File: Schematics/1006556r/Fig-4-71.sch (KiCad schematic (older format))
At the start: 0 parts

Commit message: For module A31, transcribed through Fig 4-87, leaving just 88, 91, 93, 114, 141, and 147 to go, plus their integration into the top-level sheet (and resolution of remaining inconsistencies in ND-1021041).
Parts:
- added J1: ConnectorGeneric, symbol AGC_DSKY:ConnectorGeneric
- added U? (x6): D3NOR-+3VDC-0VDC-nd1021041-ABC-___, symbol D3NOR-+3VDC-0VDC-nd1021041:D3NOR-+3VDC-0VDC-nd1021041-ABC-___
- added U? (x6): D3NOR-+3VDC-0VDC-nd1021041-A_C-___, symbol D3NOR-+3VDC-0VDC-nd1021041:D3NOR-+3VDC-0VDC-nd1021041-A_C-___
- added U? (x2): D3NOR-NC-0VDC-expander-nd1021041-A_C-___, symbol D3NOR-NC-0VDC-expander-nd1021041:D3NOR-NC-0VDC-expander-nd1021041-A_C-___
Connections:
- net +3VDC: now also U?.6 (+3VDC), U?.6 (+3VDC), U?.6 (+3VDC), U?.6 (+3VDC), U?.6 (+3VDC), U?.6 (+3VDC), U?.6 (+3VDC), U?.6 (+3VDC), U?.6 (+3VDC), U?.6 (+3VDC), U?.6 (+3VDC), U?.6 (+3VDC)
- net 0VDC: now also U?.3 (0VDC), U?.3 (0VDC), U?.3 (0VDC), U?.3 (0VDC), U?.3 (0VDC), U?.3 (0VDC), U?.3 (0VDC), U?.3 (0VDC), U?.5 (0VDC), U?.5 (0VDC), U?.5 (0VDC), U?.5 (0VDC), U?.5 (0VDC), U?.5 (0VDC), U?.5 (0VDC), U?.5 (0VDC), U?.5 (0VDC), U?.5 (0VDC), U?.5 (0VDC), U?.5 (0VDC), U?.5 (0VDC), U?.5 (0VDC)
- new net: U?.1 (J), U?.2 (C) (x4)
- new net: J1.116, U?.2 (C), U?.4 (A), U?.4 (A)
- new net: J1.118, U?.3 (B), U?.3 (B)
- new net: J1.60, U?.3 (B), U?.4 (A)
- new net: J1.33, U?.2 (C)
- new net: J1.112, U?.2 (C)
- new net: U?.1 (J), U?.4 (A) (x2)
- new net: J1.102, U?.2 (C), U?.2 (C)
- new net: J1.123, U?.2 (C), U?.2 (C)
- new net: J1.137, U?.4 (A)
- new net: J1.139, U?.4 (A)
- new net: J1.89, U?.3 (B)
- new net: J1.41, U?.4 (A)
- new net: J1.66, U?.1 (J)
- new net: J1.111, U?.2 (C)
- new net: U?.1 (J), U?.3 (B) (x2)
- new net: J1.136, U?.4 (A), U?.4 (A)
- new net: J1.121, U?.1 (J), U?.4 (A)
- new net: J1.127, U?.2 (C)
- new net: J1.74, U?.2 (C)
- new net: J1.110, U?.1 (J), U?.1 (J)
- new net: J1.108, U?.4 (A)
- new net: J1.129, U?.1 (J)
- new net PIN107: J1.107, U?.1 (J)

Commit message: Finished up transcription of drawing 1006556 (Block I logic flow S, module A21).  But it may be a total mess, so user beware!
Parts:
- removed unit 112 of J1
- removed unit 116 of J1
- removed unit 139 of J1
- removed unit 89 of J1
- removed unit 137 of J1
- removed unit 60 of J1
- removed unit 41 of J1
- removed unit 136 of J1
- removed unit 33 of J1
- removed unit 102 of J1
- removed unit 121 of J1
- removed unit 123 of J1
- removed unit 74 of J1
- removed unit 118 of J1
- removed U? (x3): D3NOR-+3VDC-0VDC-nd1021041-A_C-___, symbol D3NOR-+3VDC-0VDC-nd1021041:D3NOR-+3VDC-0VDC-nd1021041-A_C-___
- gave numbers to parts that had none: 11
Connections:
- net g60074: now reaches U1108.1 (J), U1110.2 (C)
- net T05_B: now reaches U1102.4 (A), U1108.2 (C), U1109.4 (A)
- net DV0_: now reaches U1108.3 (B), U1109.3 (B)
- net BR1_: now reaches U1107.3 (B), U1108.4 (A)
- net g60075: now reaches U1102.1 (J), U1105.2 (C)
- net DV1_: now reaches U1102.2 (C)
- net g60070: now reaches U1105.4 (A)
- net MP0_: now reaches U1107.2 (C)
- net g60071: now reaches U1103.1 (J), U1104.2 (C)
- net MP1_: now reaches U1103.2 (C)
- net T05_: now reaches U1103.4 (A)
- net T04_B: now reaches U1106.4 (A)
- net BR1: now reaches U1106.3 (B)
- net BR1: now also U1109.2 (C)
- net T02_: now reaches U1101.4 (A)
- net g60059: now reaches U1107.1 (J), U1110.3 (B)
- net T04_: now reaches U1107.4 (A)
- net g60037: now reaches U1104.4 (A)
- net g60038: now reaches U1101.1 (J), U1104.3 (B)
- net g60073: now reaches U1109.1 (J), U1111.4 (A)
- net g60060: now reaches U1111.2 (C)

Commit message: When I started recovering transcribed Block I schematics from document ND-1021041, there was no info available to me on the pinout of the NOR-gates they used, and it didn't occur to me that any might be forthcoming, so I chose a pinout arbitrarily.  It turns out that we now have the required info (SCD 1006771), and my arbitrary choices were wrong. I've therefore updated the NOR-library generator script, the relevant NOR libraries themselves, and all of the so-far-recovered Block I schematics using those gates.  It doesn't really matter in the cosmic sense, since the real Block I schematics have become available in the meantime, so that these recovered schematics are of less interest, but it will come in handy when I eventually want to do cross-checking.  I haven't checked these updated schematics in full detail, but I've spot-checked them, and run some ERCs and netlists, and it looks good to me.
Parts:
- U1101, U1102, U1103: value D3NOR-+3VDC-0VDC-nd1021041-A_C-___ -> D3NOR-+3VDC-0VDC-nd1021041-1_5-___; symbol D3NOR-+3VDC-0VDC-nd1021041:D3NOR-+3VDC-0VDC-nd1021041-A_C-___ -> D3NOR-+3VDC-0VDC-nd1021041:D3NOR-+3VDC-0VDC-nd1021041-1_5-___
- U1104, U1106, U1107, U1108, U1109, U1110: value D3NOR-+3VDC-0VDC-nd1021041-ABC-___ -> D3NOR-+3VDC-0VDC-nd1021041-135-___; symbol D3NOR-+3VDC-0VDC-nd1021041:D3NOR-+3VDC-0VDC-nd1021041-ABC-___ -> D3NOR-+3VDC-0VDC-nd1021041:D3NOR-+3VDC-0VDC-nd1021041-135-___
- U1105, U1111: value D3NOR-NC-0VDC-expander-nd1021041-A_C-___ -> D3NOR-NC-0VDC-expander-nd1021041-1_5-___; symbol D3NOR-NC-0VDC-expander-nd1021041:D3NOR-NC-0VDC-expander-nd1021041-A_C-___ -> D3NOR-NC-0VDC-expander-nd1021041:D3NOR-NC-0VDC-expander-nd1021041-1_5-___
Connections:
- net +3VDC: now also U1101.8 (+3VDC), U1102.8 (+3VDC), U1103.8 (+3VDC), U1104.8 (+3VDC), U1106.8 (+3VDC), U1107.8 (+3VDC), U1108.8 (+3VDC), U1109.8 (+3VDC), U1110.8 (+3VDC); no longer U1101.6 (+3VDC), U1102.6 (+3VDC), U1103.6 (+3VDC), U1104.6 (+3VDC), U1106.6 (+3VDC), U1107.6 (+3VDC), U1108.6 (+3VDC), U1109.6 (+3VDC), U1110.6 (+3VDC)
- net 0VDC: now also U1101.4 (0VDC), U1102.4 (0VDC), U1103.4 (0VDC), U1104.4 (0VDC), U1105.4 (0VDC), U1106.4 (0VDC), U1107.4 (0VDC), U1108.4 (0VDC), U1109.4 (0VDC), U1110.4 (0VDC), U1111.4 (0VDC); no longer U1101.5 (0VDC), U1102.5 (0VDC), U1103.5 (0VDC), U1104.5 (0VDC), U1105.5 (0VDC), U1106.5 (0VDC), U1107.5 (0VDC), U1108.5 (0VDC), U1109.5 (0VDC), U1110.5 (0VDC), U1111.5 (0VDC)
- net BR1: now also U1109.5; no longer U1109.2 (C)
- net BR1_: now also U1108.1; no longer U1108.4 (A)
- net DV1_: now also U1102.5; no longer U1102.2 (C)
- net MP0_: now also U1107.5; no longer U1107.2 (C)
- net MP1_: now also U1103.5; no longer U1103.2 (C)
- net PIN107: now also U1106.7; no longer U1106.1 (J)
- net T02_: now also U1101.1; no longer U1101.4 (A)
- net T04_: now also U1107.1; no longer U1107.4 (A)
- net T04_B: now also U1106.1; no longer U1106.4 (A)
- net T05_: now also U1103.1; no longer U1103.4 (A)
- net T05_B: now also U1102.1, U1108.5, U1109.1; no longer U1102.4 (A), U1108.2 (C), U1109.4 (A)
- net g60037: now also U1104.1; no longer U1104.4 (A)
- net g60038: now also U1101.7; no longer U1101.1 (J)
- net g60059: now also U1107.7; no longer U1107.1 (J)
- net g60060: now also U1111.5; no longer U1111.2 (C)
- net g60070: now also U1105.1; no longer U1105.4 (A)
- net g60071: now also U1103.7, U1104.5; no longer U1103.1 (J), U1104.2 (C)
- net g60073: now also U1109.7, U1111.1; no longer U1109.1 (J), U1111.4 (A)
- net g60074: now also U1108.7, U1110.5; no longer U1108.1 (J), U1110.2 (C)
- net g60075: now also U1102.7, U1105.5; no longer U1102.1 (J), U1105.2 (C)
- net at J1.66: now also U1105.7; no longer U1105.1 (J)
- net at U1106.2 (NC): no longer J1.111
- net at U1101.2 (NC): no longer J1.127
- net at J1.108: now also U1110.1; no longer U1110.4 (A)
- net at J1.129: now also U1104.7; no longer U1104.1 (J)
- new net: J1.111, U1106.5
- new net: J1.127, U1101.5
- new net: J1.110, U1110.7, U1111.7
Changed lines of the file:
@@
 0VDC
 $Comp
-L D3NOR-+3VDC-0VDC-nd1021041:D3NOR-+3VDC-0VDC-nd1021041-ABC-___ U1108
+L D3NOR-+3VDC-0VDC-nd1021041:D3NOR-+3VDC-0VDC-nd1021041-135-___ U1108
 U 1 1 5BFA9681
 P 14725 8150
 F 0 "U1108" H 14725 8475 140 0001 C CNB
-F 1 "D3NOR-+3VDC-0VDC-nd1021041-ABC-___" H 14725 8575 140 0001 C CNN
+F 1 "D3NOR-+3VDC-0VDC-nd1021041-135-___" H 14725 8575 140 0001 C CNN
 F 2 "" H 14725 8625 140 0001 C CNN
 F 3 "" H 14725 8625 140 0001 C CNN
@@
 $EndComp
 $Comp
-L D3NOR-+3VDC-0VDC-nd1021041:D3NOR-+3VDC-0VDC-nd1021041-A_C-___ U1102
+L D3NOR-+3VDC-0VDC-nd1021041:D3NOR-+3VDC-0VDC-nd1021041-1_5-___ U1102
 U 1 1 5BFA9682
 P 4650 11275
 F 0 "U1102" H 4650 11600 140 0001 C CNB
-F 1 "D3NOR-+3VDC-0VDC-nd1021041-A_C-___" H 4650 11700 140 0001 C CNN
+F 1 "D3NOR-+3VDC-0VDC-nd1021041-1_5-___" H 4650 11700 140 0001 C CNN
 F 2 "" H 4650 11750 140 0001 C CNN
 F 3 "" H 4650 11750 140 0001 C CNN
@@
 $EndComp
 $Comp
-L D3NOR-+3VDC-0VDC-nd1021041:D3NOR-+3VDC-0VDC-nd1021041-A_C-___ U1103
+L D3NOR-+3VDC-0VDC-nd1021041:D3NOR-+3VDC-0VDC-nd1021041-1_5-___ U1103
 U 1 1 5BFA9685
 P 4675 8075
 F 0 "U1103" H 4675 8400 140 0001 C CNB
-F 1 "D3NOR-+3VDC-0VDC-nd1021041-A_C-___" H 4675 8500 140 0001 C CNN
+F 1 "D3NOR-+3VDC-0VDC-nd1021041-1_5-___" H 4675 8500 140 0001 C CNN
 F 2 "" H 4675 8550 140 0001 C CNN
 F 3 "" H 4675 8550 140 0001 C CNN
@@
 $EndComp
 $Comp
-L D3NOR-+3VDC-0VDC-nd1021041:D3NOR-+3VDC-0VDC-nd1021041-ABC-___ U1106
+L D3NOR-+3VDC-0VDC-nd1021041:D3NOR-+3VDC-0VDC-nd1021041-135-___ U1106
 U 1 1 5BFA968D
 P 14725 4950
 F 0 "U1106" H 14725 5275 140 0001 C CNB
-F 1 "D3NOR-+3VDC-0VDC-nd1021041-ABC-___" H 14725 5375 140 0001 C CNN
+F 1 "D3NOR-+3VDC-0VDC-nd1021041-135-___" H 14725 5375 140 0001 C CNN
 F 2 "" H 14725 5425 140 0001 C CNN
 F 3 "" H 14725 5425 140 0001 C CNN
@@
 $EndComp
 $Comp
-L D3NOR-+3VDC-0VDC-nd1021041:D3NOR-+3VDC-0VDC-nd1021041-ABC-___ U1107
+L D3NOR-+3VDC-0VDC-nd1021041:D3NOR-+3VDC-0VDC-nd1021041-135-___ U1107
 U 1 1 5BFA968E
 P 14725 6575
 F 0 "U1107" H 14725 6900 140 0001 C CNB
-F 1 "D3NOR-+3VDC-0VDC-nd1021041-ABC-___" H 14725 7000 140 0001 C CNN
+F 1 "D3NOR-+3VDC-0VDC-nd1021041-135-___" H 14725 7000 140 0001 C CNN
 F 2 "" H 14725 7050 140 0001 C CNN
 F 3 "" H 14725 7050 140 0001 C CNN
@@
 $EndComp
 $Comp
-L D3NOR-+3VDC-0VDC-nd1021041:D3NOR-+3VDC-0VDC-nd1021041-A_C-___ U1101
+L D3NOR-+3VDC-0VDC-nd1021041:D3NOR-+3VDC-0VDC-nd1021041-1_5-___ U1101
 U 1 1 5BFA9690
 P 4650 6500
 F 0 "U1101" H 4650 6825 140 0001 C CNB
-F 1 "D3NOR-+3VDC-0VDC-nd1021041-A_C-___" H 4650 6925 140 0001 C CNN
+F 1 "D3NOR-+3VDC-0VDC-nd1021041-1_5-___" H 4650 6925 140 0001 C CNN
 F 2 "" H 4650 6975 140 0001 C CNN
 F 3 "" H 4650 6975 140 0001 C CNN
@@
 $EndComp
 $Comp
-L D3NOR-+3VDC-0VDC-nd1021041:D3NOR-+3VDC-0VDC-nd1021041-ABC-___ U1109
+L D3NOR-+3VDC-0VDC-nd1021041:D3NOR-+3VDC-0VDC-nd1021041-135-___ U1109
 U 1 1 5BFA9691
 P 14725 9750
 F 0 "U1109" H 14725 10075 140 0001 C CNB
-F 1 "D3NOR-+3VDC-0VDC-nd1021041-ABC-___" H 14725 10175 140 0001 C CNN
+F 1 "D3NOR-+3VDC-0VDC-nd1021041-135-___" H 14725 10175 140 0001 C CNN
 F 2 "" H 14725 10225 140 0001 C CNN
 F 3 "" H 14725 10225 140 0001 C CNN
@@
 $EndComp
 $Comp
-L D3NOR-NC-0VDC-expander-nd1021041:D3NOR-NC-0VDC-expander-nd1021041-A_C-___ U1111
+L D3NOR-NC-0VDC-expander-nd1021041:D3NOR-NC-0VDC-expander-nd1021041-1_5-___ U1111
 U 1 1 5BFA9693
 P 18625 8900
 F 0 "U1111" H 18625 9225 140 0001 C CNB
-F 1 "D3NOR-NC-0VDC-expander-nd1021041-A_C-___" H 18625 9325 140 0001 C CNN
+F 1 "D3NOR-NC-0VDC-expander-nd1021041-1_5-___" H 18625 9325 140 0001 C CNN
 F 2 "" H 18625 9375 140 0001 C CNN
 F 3 "" H 18625 9375 140 0001 C CNN
@@
 $EndComp
 $Comp
-L D3NOR-+3VDC-0VDC-nd1021041:D3NOR-+3VDC-0VDC-nd1021041-ABC-___ U1110
+L D3NOR-+3VDC-0VDC-nd1021041:D3NOR-+3VDC-0VDC-nd1021041-135-___ U1110
 U 1 1 5BFA9694
 P 18625 7800
 F 0 "U1110" H 18625 8125 140 0001 C CNB
-F 1 "D3NOR-+3VDC-0VDC-nd1021041-ABC-___" H 18625 8225 140 0001 C CNN
+F 1 "D3NOR-+3VDC-0VDC-nd1021041-135-___" H 18625 8225 140 0001 C CNN
 F 2 "" H 18625 8275 140 0001 C CNN
 F 3 "" H 18625 8275 140 0001 C CNN
@@
 $EndComp
 $Comp
-L D3NOR-+3VDC-0VDC-nd1021041:D3NOR-+3VDC-0VDC-nd1021041-ABC-___ U1104
+L D3NOR-+3VDC-0VDC-nd1021041:D3NOR-+3VDC-0VDC-nd1021041-135-___ U1104
 U 1 1 5BFA96A2
 P 7750 7725
 F 0 "U1104" H 7750 8050 140 0001 C CNB
-F 1 "D3NOR-+3VDC-0VDC-nd1021041-ABC-___" H 7750 8150 140 0001 C CNN
+F 1 "D3NOR-+3VDC-0VDC-nd1021041-135-___" H 7750 8150 140 0001 C CNN
 F 2 "" H 7750 8200 140 0001 C CNN
 F 3 "" H 7750 8200 140 0001 C CNN
@@
 $EndComp
 $Comp
-L D3NOR-NC-0VDC-expander-nd1021041:D3NOR-NC-0VDC-expander-nd1021041-A_C-___ U1105
+L D3NOR-NC-0VDC-expander-nd1021041:D3NOR-NC-0VDC-expander-nd1021041-1_5-___ U1105
 U 1 1 5BFA96A3
 P 7750 8850
 F 0 "U1105" H 7750 9175 140 0001 C CNB
-F 1 "D3NOR-NC-0VDC-expander-nd1021041-A_C-___" H 7750 9275 140 0001 C CNN
+F 1 "D3NOR-NC-0VDC-expander-nd1021041-1_5-___" H 7750 9275 140 0001 C CNN
 F 2 "" H 7750 9325 140 0001 C CNN
 F 3 "" H 7750 9325 140 0001 C CNN

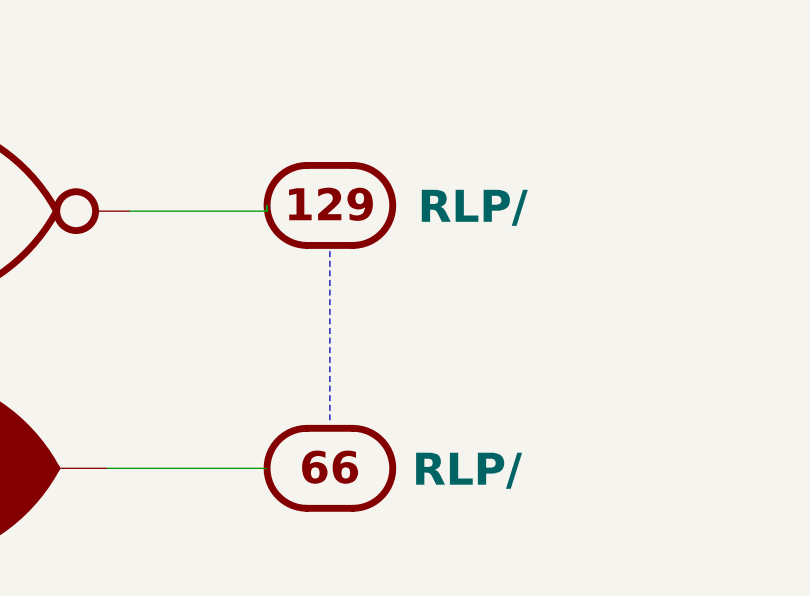
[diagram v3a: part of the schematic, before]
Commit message: Fixed up netlistCompare.py, as well as several bugs in both 1006556A and r.  There are still bugs to fix in them, as well as actual structural mismatches to document, but I'm making progress.
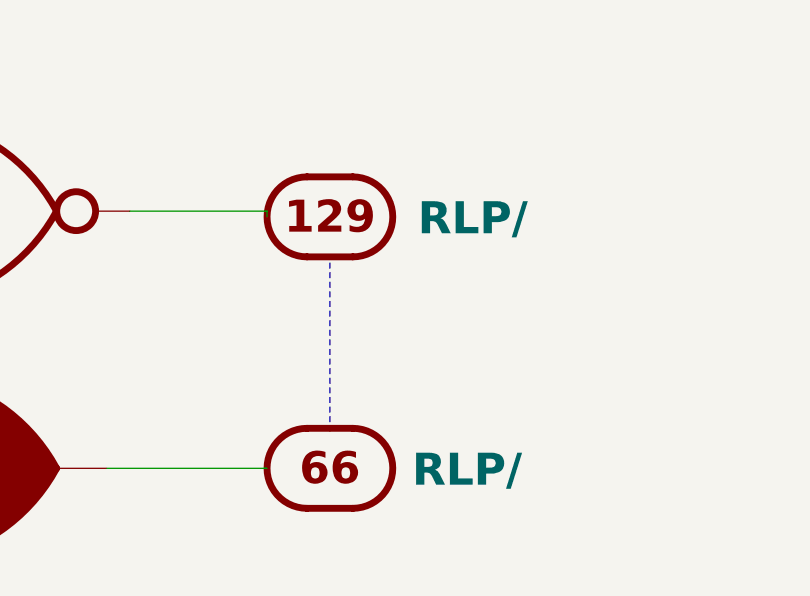
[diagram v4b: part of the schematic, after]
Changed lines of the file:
@@
 L AGC_DSKY:ConnectorGeneric J1
 U 129 1 5BFA9696
-P 9525 7700
-F 0 "J1" H 9525 8025 140 0001 C CNN
-F 1 "ConnectorGeneric" H 9525 8125 140 0001 C CNN
-F 2 "" H 9525 8175 140 0001 C CNN
-F 3 "" H 9525 8175 140 0001 C CNN
-F 4 "RLP/" H 8900 7625 140 0000 C BNB "Caption"
-	129  9525 7700
+P 9525 7750
+F 0 "J1" H 9525 8075 140 0001 C CNN
+F 1 "ConnectorGeneric" H 9525 8175 140 0001 C CNN
+F 2 "" H 9525 8225 140 0001 C CNN
+F 3 "" H 9525 8225 140 0001 C CNN
+F 4 "RLP/" H 8900 7675 140 0000 C BNB "Caption"
+	129  9525 7750
 	-1   0    0    1
 $EndComp
@@
 	8650 7725 9250 7725
 Wire Wire Line
-	9250 7725 9250 7700
+	9250 7725 9250 7750
 Wire Wire Line
 	8550 8850 9250 8850
@@
 	6100 8500 7125 8500
 Wire Notes Line
-	9525 7900 9525 8650
+	9525 7950 9525 8700
 Wire Wire Line
 	5550 11275 5700 11275

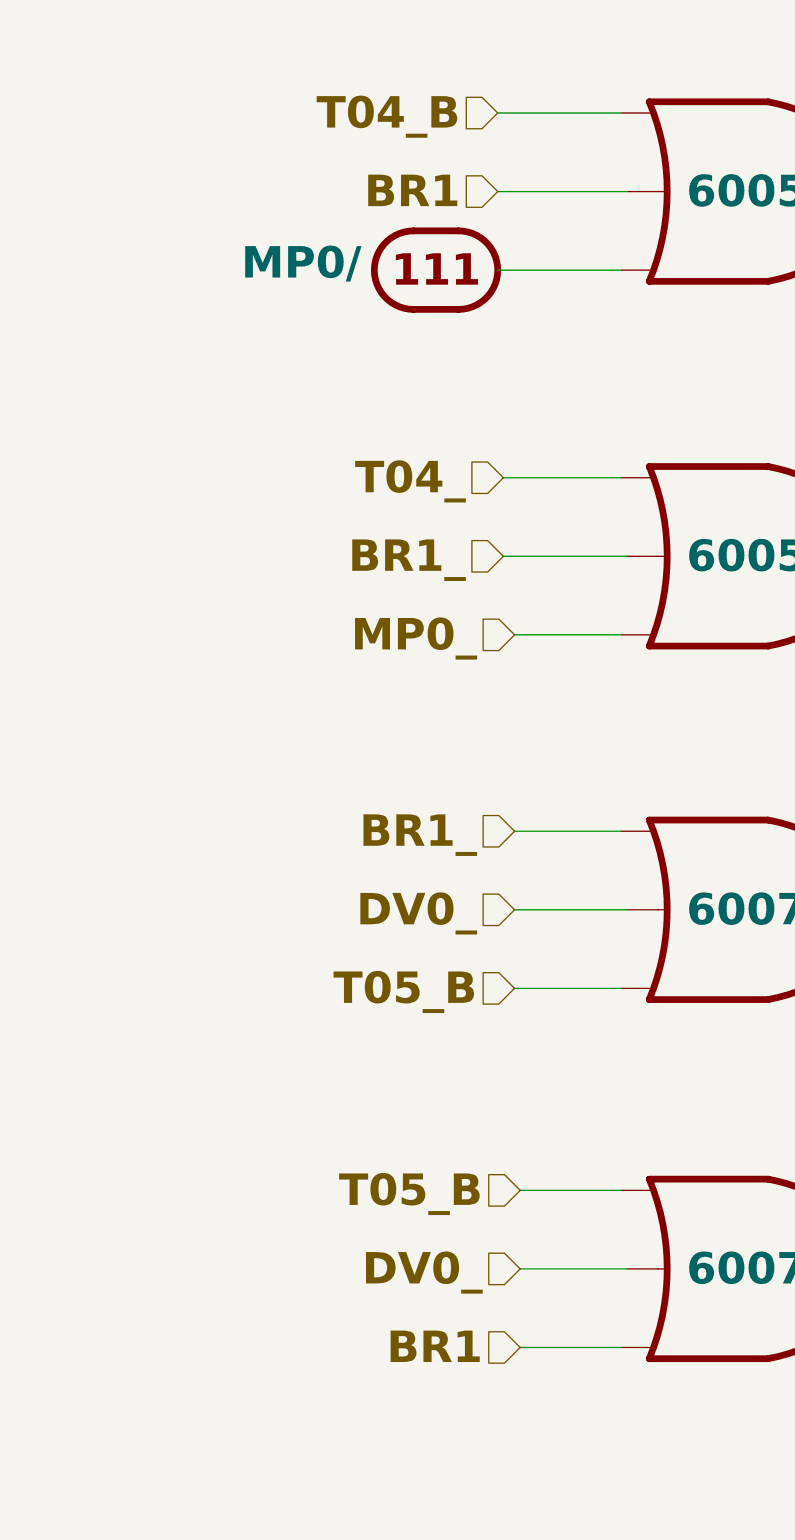
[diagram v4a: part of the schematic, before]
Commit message: Schematics 1006556r and 1006556A have been cross-checked and corrected, insofar as it is possible to do so, given that 1006556r (from ND-1021041) appears to be a later revision with some electrical changes.
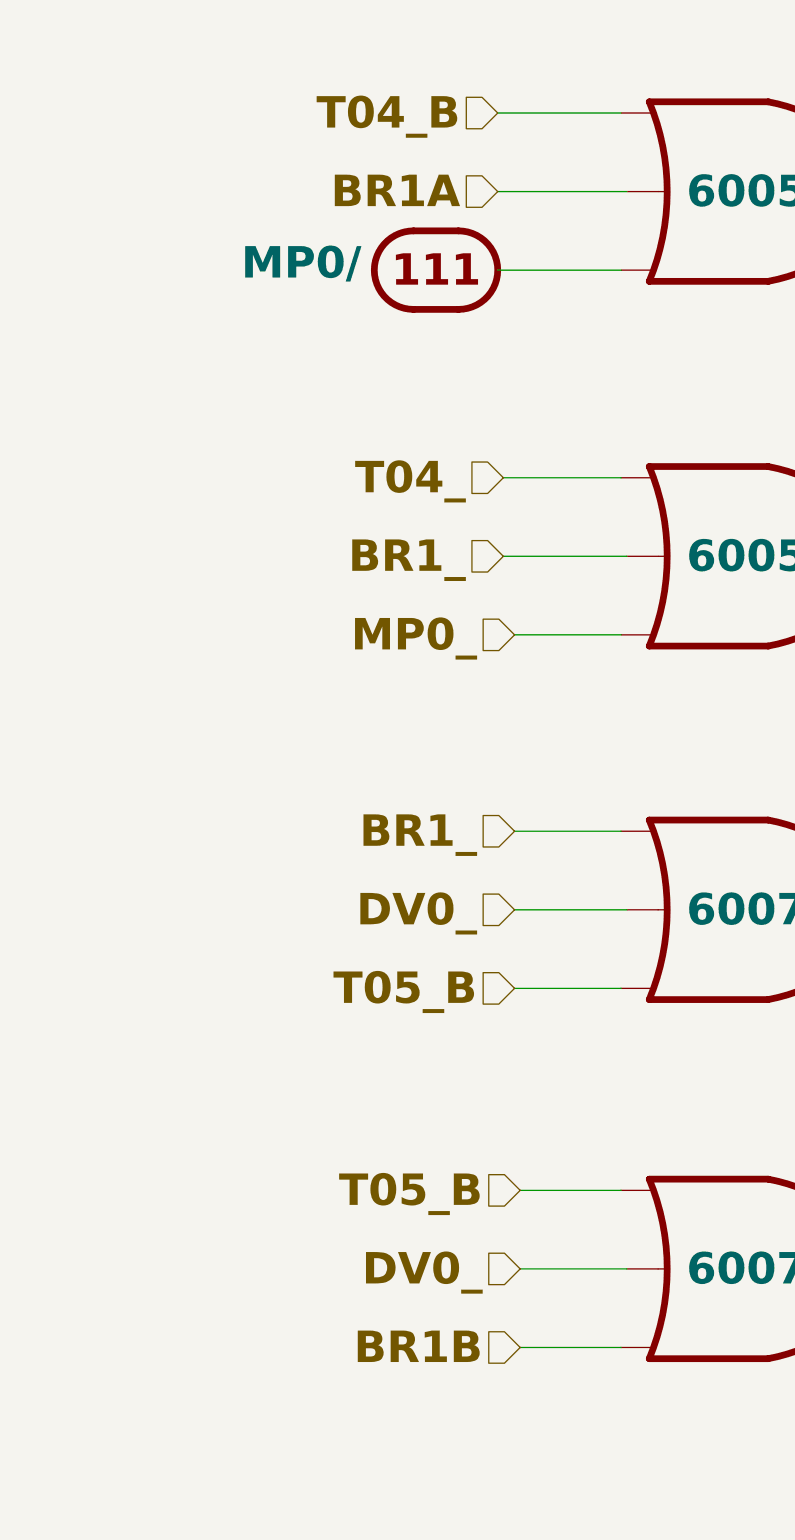
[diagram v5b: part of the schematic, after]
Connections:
- net BR1 renamed BR1A
- net BR1A: no longer U1109.5
- new net BR1B: U1109.5
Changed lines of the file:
@@
 $Descr C 22000 17000
 encoding utf-8
-Sheet 11 24
+Sheet 24 24
 Title "BLOCK I LOGIC FLOW S, MODULE A21, DRAWING 1006556"
 Date "2018-11-25"
@@
 MP0_
 Text HLabel 13550 4950 0    140  Input ~ 28
-BR1
+BR1A
 Text HLabel 13650 10100 0    140  Input ~ 28
-BR1
+BR1B
 Text HLabel 3475 6150 0    140  Input ~ 28
 T02_
